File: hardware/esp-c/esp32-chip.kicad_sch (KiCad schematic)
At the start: 26 parts, among them U12 ESP32-WROOM-32E(4MB), U3 SS8050_C2150, U8 SS8050_C2150

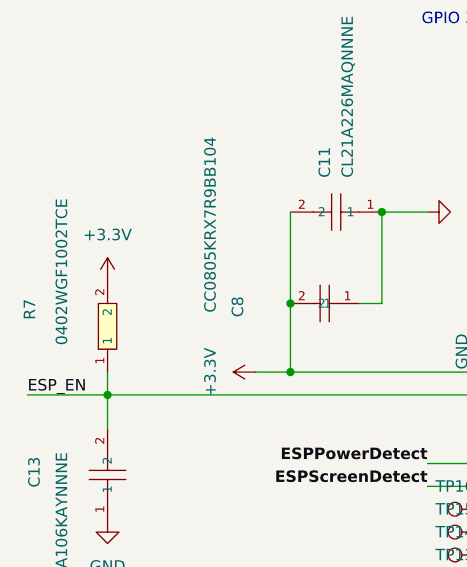
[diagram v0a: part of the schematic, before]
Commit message: Update component R7 to use 0805 package instead of 0402. Tweak some associated traces.
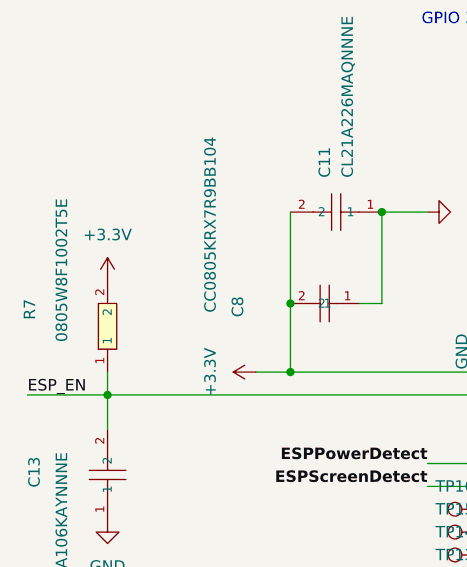
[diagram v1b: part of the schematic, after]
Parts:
- R7: value 0402WGF1002TCE -> 0805W8F1002T5E; footprint JLCPCB_footprint:R0402 -> JLCPCB_footprint:R0805; LCSC C25744 -> C17414
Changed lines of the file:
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@@
 			)
 		)
-		(property "Value" "0402WGF1002TCE"
+		(property "Value" "0805W8F1002T5E"
 			(at 22.86 50.546 0)
 			(effects
@@
 			)
 		)
-		(property "Footprint" "JLCPCB_footprint:R0402"
+		(property "Footprint" "JLCPCB_footprint:R0805"
 			(at 38.1 64.77 0)
 			(effects
@@
 			)
 		)
-		(property "Datasheet" "https://item.szlcsc.com/323315.html"
+		(property "Datasheet" "https://jlcpcb.com/partdetail/18102-0805W8F1002T5E/C17414"
 			(at 27.813 67.056 0)
 			(effects
@@
 			)
 		)
-		(property "LCSC" "C25744"
+		(property "LCSC" "C17414"
 			(at 27.94 64.77 0)
 			(effects
